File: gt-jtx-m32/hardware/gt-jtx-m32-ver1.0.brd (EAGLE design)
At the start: 59.4 x 64.8 mm, 29 parts, among them IC1 MEGA32-P

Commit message: updated
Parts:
- removed AD0, AD1, AD2, AD3, AD4, AD5, AD6, AD7, D0, D1, D2, D3, D4, D5, D6, D7: (no value), pinhead:1X03
- removed GNDC, TRIMS: (no value), pinhead:1X08
- removed LED: (no value), led:LED5MM
- removed PWR: (no value), pinhead:1X02
- removed R2: (no value), resistor:0204V
- added AIL, CH4, CH5, CH6, CH7, CH8, ELE, RUD, THR: (no value), Rembrandt Electronics - JST XH Connectors v1-0:JST-XH-03-PACKAGE-LONG-PAD
- added TRIM: TRIM, Rembrandt Electronics - JST XH Connectors v1-0:JST-XH-08-PACKAGE-LONG-PAD
- added X1, X2, X3, X4, X5, X6, X7: JST-XH-03-PIN-LONG-PAD, Rembrandt Electronics - JST XH Connectors v1-0:JST-XH-03-PACKAGE-LONG-PAD
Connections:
- removed net +5V: AD0.2, AD1.2, AD2.2, AD3.2, AD4.2, AD5.2, AD6.2, AD7.2, D0.2, D1.2, D2.2, D3.2, D4.2, D5.2, D6.2, D7.2, IC1.10, IC1.30, IC1.32, ISP.2, LED.A, PPM.2, PWR.1, R2.1, USART.4
- removed net GND: AD0.1, AD1.1, AD2.1, AD3.1, AD4.1, AD5.1, AD6.1, AD7.1, D0.1, D1.1, D2.1, D3.1, D4.1, D5.1, D6.1, D7.1, GNDC.1, GNDC.2, GNDC.3, GNDC.4, GNDC.5, GNDC.6, GNDC.7, GNDC.8, IC1.11, IC1.31, ISP.6, JP3.1, JP4.1, LED.K, PPM.3, PWR.2, USART.1
- removed net N$18: IC1.27, TRIMS.3
- removed net N$19: IC1.26, TRIMS.4
- removed net N$20: IC1.25, TRIMS.5
- removed net N$21: IC1.24, TRIMS.6
- removed net N$22: IC1.23, TRIMS.7
- removed net N$23: IC1.22, TRIMS.8
- new net N$34: IC1.11, IC1.31, ISP.6, JP3.1, JP4.1, PPM.3, USART.1, X1.1, X2.1, X3.1, X4.1, X5.1, X6.1, X7.1
- new net N$35: ELE.3, IC1.34
- new net N$36: IC1.10, IC1.30, IC1.32, ISP.2, PPM.2, USART.4, X1.2, X2.2, X3.2, X4.2, X5.2, X6.2, X7.2
- new net N$37: IC1.35, THR.3
- new net N$38: IC1.36, RUD.3
- new net N$39: CH4.3, IC1.37
- new net N$40: CH5.3, IC1.38
- new net N$41: CH7.3, IC1.40
- net N$1: now also AIL.3, IC1.33; no longer AD7.3, IC1.40
- net N$10: now also IC1.25, TRIM.5; no longer AD2.3, IC1.35
- net N$11: now also IC1.24, TRIM.6; no longer AD1.3, IC1.34
- net N$16: now also IC1.23, TRIM.7; no longer IC1.28, TRIMS.2
- net N$17: now also IC1.22, TRIM.8; no longer AD0.3, IC1.33
- net N$2: now also CH6.3; no longer AD6.3
- net N$24: now also X5.3; no longer D3.3
- net N$25: now also X4.3; no longer D4.3
- net N$26: now also X3.3; no longer D5.3
- net N$27: now also X2.3; no longer D6.3
- net N$28: now also X1.3; no longer D7.3
- net N$29: now also X6.3; no longer D2.3
- net N$3: now also IC1.29, TRIM.1; no longer AD5.3, IC1.38
- net N$30: now also X7.3; no longer D1.3
- net N$31: now also CH8.3; no longer D0.3
- net N$4: now also IC1.28, TRIM.2; no longer AD4.3, IC1.37
- net N$7: now also IC1.27, TRIM.3; no longer IC1.29, TRIMS.1
- net N$8: now also IC1.26, TRIM.4; no longer AD3.3, IC1.36
- net N$9: no longer R2.2
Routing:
- net GND: track 231.3 -> 0.00 mm
- net +5V: track 229.5 -> 0.00 mm
- net N$12: track 27.3 -> 0.00 mm
- net N$31: track 25.5 -> 0.00 mm
- net N$29: track 20.4 -> 0.00 mm
- net N$15: track 19.4 -> 0.00 mm
- net N$24: track 18.8 -> 0.00 mm
- net N$30: track 18.8 -> 0.00 mm
- net N$28: track 18.8 -> 0.00 mm
- net N$27: track 18.3 -> 0.00 mm
- net N$25: track 18.3 -> 0.00 mm
- net N$26: track 17.8 -> 0.00 mm
- net N$32: track 13.2 -> 0.00 mm
- net N$9: track 8.89 -> 0.00 mm
- net N$6: track 8.89 -> 0.00 mm
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
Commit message: updated board design for new firmware mechanics with oled
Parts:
- removed CH8: (no value), Rembrandt Electronics - JST XH Connectors v1-0:JST-XH-03-PACKAGE-LONG-PAD
- removed ISP: (no value), pinhead:1X06
- removed JP1, JP2, JP3, JP4: (no value), pinhead:1X01
- removed X1, X2, X3, X4, X5, X6, X7: JST-XH-03-PIN-LONG-PAD, Rembrandt Electronics - JST XH Connectors v1-0:JST-XH-03-PACKAGE-LONG-PAD
- added C1: (no value), rcl:PANASONIC_C
- added D1, D2, D3, D4, D5, D6, D7, D8: (no value), Rembrandt Electronics - JST XH Connectors v1-0:JST-XH-03-PACKAGE-LONG-PAD
- added LCD: (no value), Rembrandt Electronics - JST XH Connectors v1-0:JST-XH-04-PACKAGE-LONG-PAD
- PPM: device pinhead:1X03 -> Rembrandt Electronics - JST XH Connectors v1-0:JST-XH-03-PACKAGE-LONG-PAD
- USART: device pinhead:1X04 -> Rembrandt Electronics - JST XH Connectors v1-0:JST-XH-04-PACKAGE-LONG-PAD
- moved TRIM 277.9 mm to (38.1, 22.9), turned to 270 degrees
- moved AIL 257.9 mm to (52.1, 15.2), turned to 180 degrees
- moved ELE 249.1 mm to (52.1, 21.6), turned to 180 degrees
- moved THR 240.4 mm to (52.1, 27.9), turned to 180 degrees
- moved RUD 231.6 mm to (52.1, 34.3), turned to 180 degrees
- moved CH4 222.9 mm to (52.1, 40.6), turned to 180 degrees
- moved CH5 214.2 mm to (52.1, 47.0), turned to 180 degrees
- moved CH6 205.5 mm to (52.1, 53.3), turned to 180 degrees
- moved CH7 196.9 mm to (52.1, 59.7), turned to 180 degrees
- moved USART 15.3 mm to (20.3, 5.08), turned to 0 degrees
- moved IC1 12.5 mm to (24.1, 35.6)
- moved PPM 1.27 mm to (6.35, 5.08), turned to 0 degrees
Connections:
- removed net N$27: IC1.2, X2.3
- removed net N$28: IC1.1, X1.3
- removed net N$29: IC1.16, X6.3
- removed net N$30: IC1.17, X7.3
- removed net N$31: CH8.3, IC1.20
- removed net N$32: IC1.18, JP2.1
- removed net N$33: IC1.21, JP1.1
- removed net N$34: IC1.11, IC1.31, ISP.6, JP3.1, JP4.1, PPM.3, USART.1, X1.1, X2.1, X3.1, X4.1, X5.1, X6.1, X7.1
- removed net N$36: IC1.10, IC1.30, IC1.32, ISP.2, PPM.2, USART.4, X1.2, X2.2, X3.2, X4.2, X5.2, X6.2, X7.2
- new net GND: AIL.1, C1.-, CH4.1, CH5.1, CH6.1, CH7.1, D1.1, D2.1, D3.1, D4.1, D5.1, D6.1, D7.1, D8.1, ELE.1, IC1.11, IC1.31, LCD.1, PPM.1, RUD.1, THR.1, USART.1
- new net N$18: IC1.14, USART.3
- new net N$19: IC1.23, LCD.4
- new net N$22: IC1.22, LCD.3
- new net N$23: IC1.19, PPM.2
- new net VCC: AIL.2, C1.+, CH4.2, CH5.2, CH6.2, CH7.2, D1.2, D2.2, D3.2, D4.2, D5.2, D6.2, D7.2, D8.2, ELE.2, IC1.10, IC1.30, IC1.32, LCD.2, PPM.3, RUD.2, THR.2, USART.4
- net N$12: now also D6.3; no longer ISP.1
- net N$13: now also D7.3; no longer ISP.5
- net N$14: now also D8.3; no longer ISP.4
- net N$15: now also D2.3, IC1.2; no longer IC1.19, PPM.1
- net N$16: now also IC1.21; no longer IC1.23
- net N$17: now also IC1.20; no longer IC1.22
- net N$24: now also D3.3, IC1.3; no longer IC1.5, X5.3
- net N$25: now also D4.3; no longer X4.3
- net N$26: now also D5.3, IC1.5; no longer IC1.3, X3.3
- net N$5: now also D1.3, IC1.1; no longer IC1.14, USART.2
- net N$6: now also USART.2; no longer USART.3
- net N$9: no longer ISP.3
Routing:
- net N$1: track 0.00 -> 34.4 mm
- net N$14: track 0.00 -> 31.5 mm
- net N$35: track 0.00 -> 30.6 mm
- net N$13: track 0.00 -> 27.7 mm
- net N$37: track 0.00 -> 26.8 mm
- net N$17: track 0.00 -> 24.7 mm, vias 0 -> 1
- net N$38: track 0.00 -> 24.5 mm
- net N$18: track 0.00 -> 24.1 mm
- net N$12: track 0.00 -> 23.8 mm
- net N$39: track 0.00 -> 22.9 mm
- net N$22: track 0.00 -> 22.6 mm
- net N$40: track 0.00 -> 21.3 mm
- net N$6: track 0.00 -> 20.5 mm
- net N$26: track 0.00 -> 20.0 mm
- net N$19: track 0.00 -> 20.0 mm
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- added copper zone on layer 1, net VCC
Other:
- board text added: "v1.2"
- board text removed: "ver 1.0"

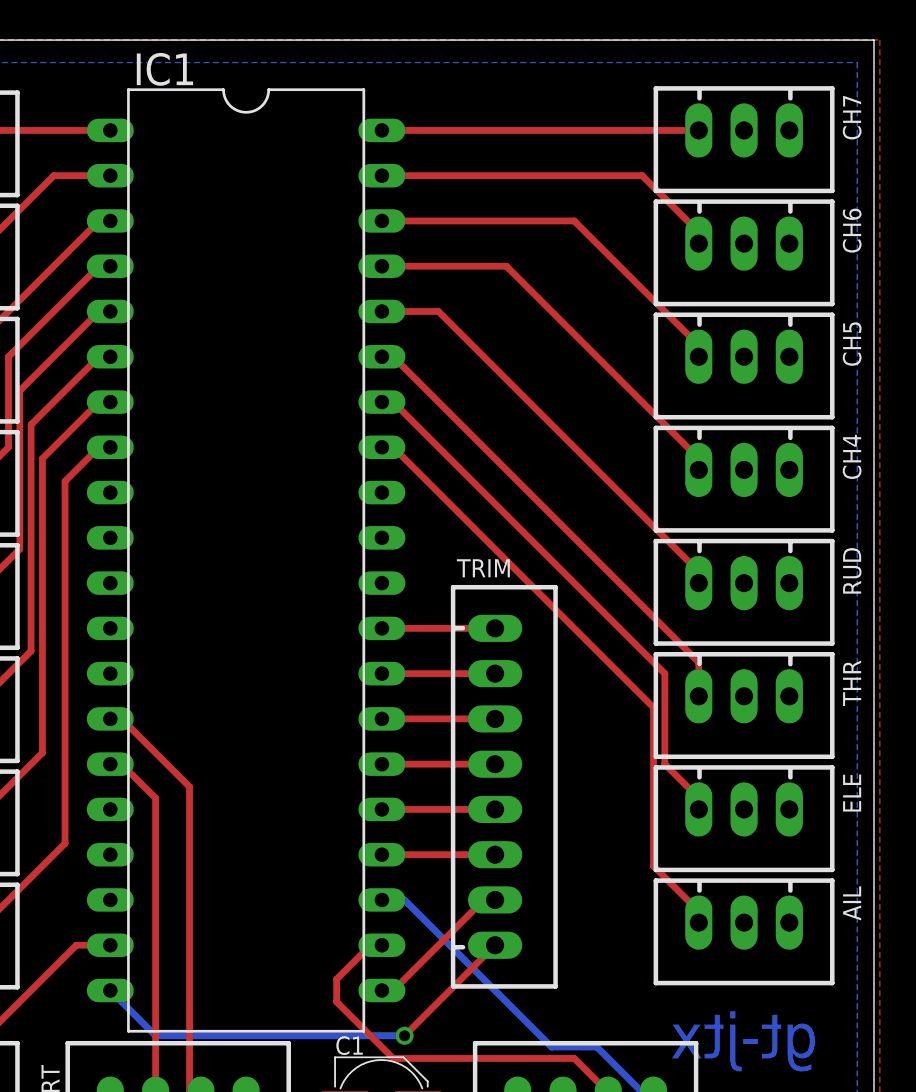
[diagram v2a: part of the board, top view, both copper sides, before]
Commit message: updated board with led and isp header updated code with newer structure of using rx/tx
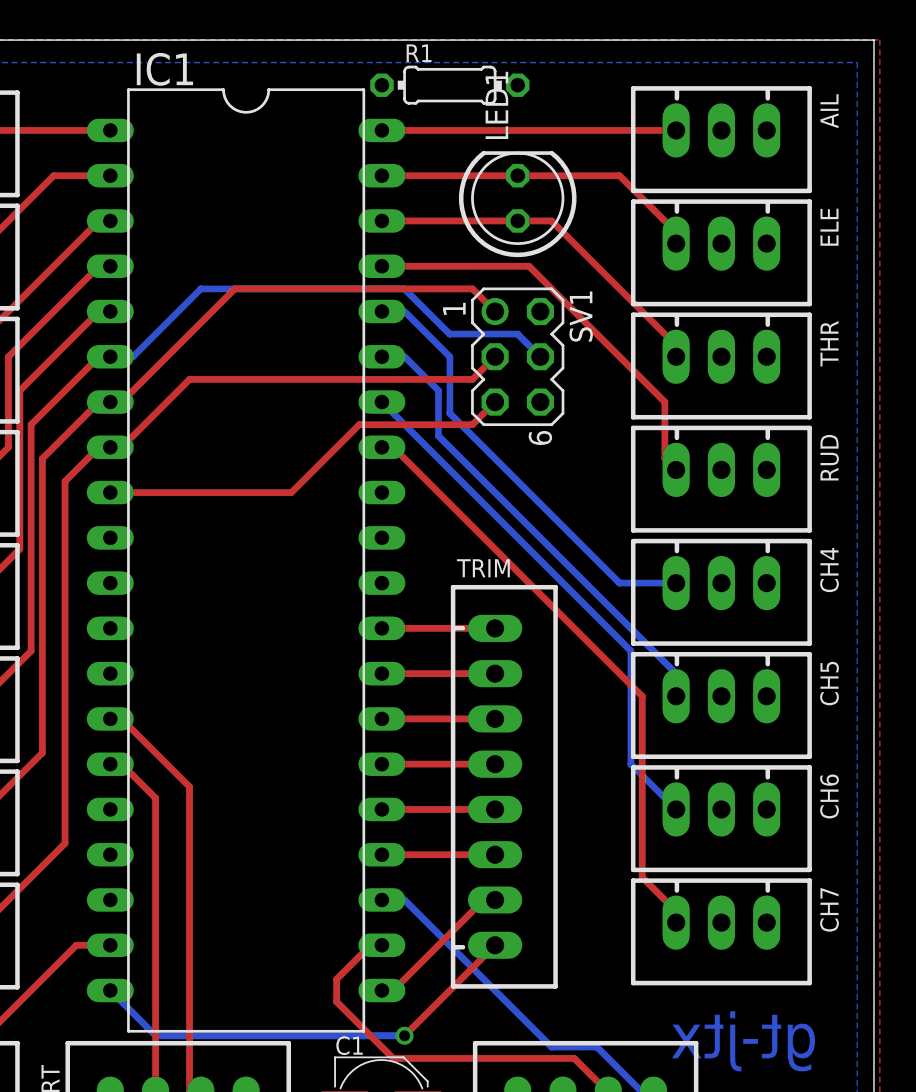
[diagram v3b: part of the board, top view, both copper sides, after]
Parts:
- added LED1: (no value), led:LED5MM
- added R1: (no value), eagle-ltspice:0204/7
- added SV1: (no value), con-lstb:MA03-2
- moved AIL 44.5 mm to (50.8, 59.7)
- moved CH7 44.5 mm to (50.8, 15.2)
- moved CH6 31.8 mm to (50.8, 21.6)
- moved ELE 31.8 mm to (50.8, 53.3)
- moved CH5 19.1 mm to (50.8, 27.9)
- moved THR 19.1 mm to (50.8, 47.0)
- moved CH4 6.48 mm to (50.8, 34.3)
- moved RUD 6.48 mm to (50.8, 40.6)
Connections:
- removed net N$35: ELE.3, IC1.34
- removed net N$37: IC1.35, THR.3
- removed net N$38: IC1.36, RUD.3
- removed net N$39: CH4.3, IC1.37
- removed net N$40: CH5.3, IC1.38
- removed net N$41: CH7.3, IC1.40
- new net N$20: CH7.3, IC1.33
- new net N$21: CH4.3, IC1.36
- new net N$27: IC1.37, RUD.3
- new net N$28: IC1.38, THR.3
- new net N$29: ELE.3, IC1.39
- new net N$30: AIL.3, IC1.40
- new net N$32: LED1.K, R1.2
- net GND: now also R1.1, SV1.6
- net N$1: now also CH5.3, IC1.35; no longer AIL.3, IC1.33
- net N$12: now also SV1.4
- net N$13: now also SV1.1
- net N$14: now also SV1.3
- net N$2: now also IC1.34; no longer IC1.39
- net N$9: now also SV1.5
- net VCC: now also LED1.A, SV1.2
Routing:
- net N$20: track 0.00 -> 33.9 mm
- net N$35: track 30.6 -> 0.00 mm
- net N$12: track 23.8 -> 51.1 mm
- net N$37: track 26.8 -> 0.00 mm
- net N$13: track 27.7 -> 52.4 mm
- net N$21: track 0.00 -> 24.7 mm
- net N$38: track 24.5 -> 0.00 mm
- net N$9: track 0.00 -> 23.7 mm
- net N$14: track 31.5 -> 55.2 mm
- net N$27: track 0.00 -> 23.1 mm
- net N$39: track 22.9 -> 0.00 mm
- net N$40: track 21.3 -> 0.00 mm
- net N$28: track 0.00 -> 20.0 mm
- net N$29: track 0.00 -> 18.5 mm
- net N$41: track 17.8 -> 0.00 mm
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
